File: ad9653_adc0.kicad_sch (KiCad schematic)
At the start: 20 parts, among them J201 142-0701-201, J202 142-0701-201, J203 142-0701-201, J204 142-0701-201, U201 AD9653BCPZ-125

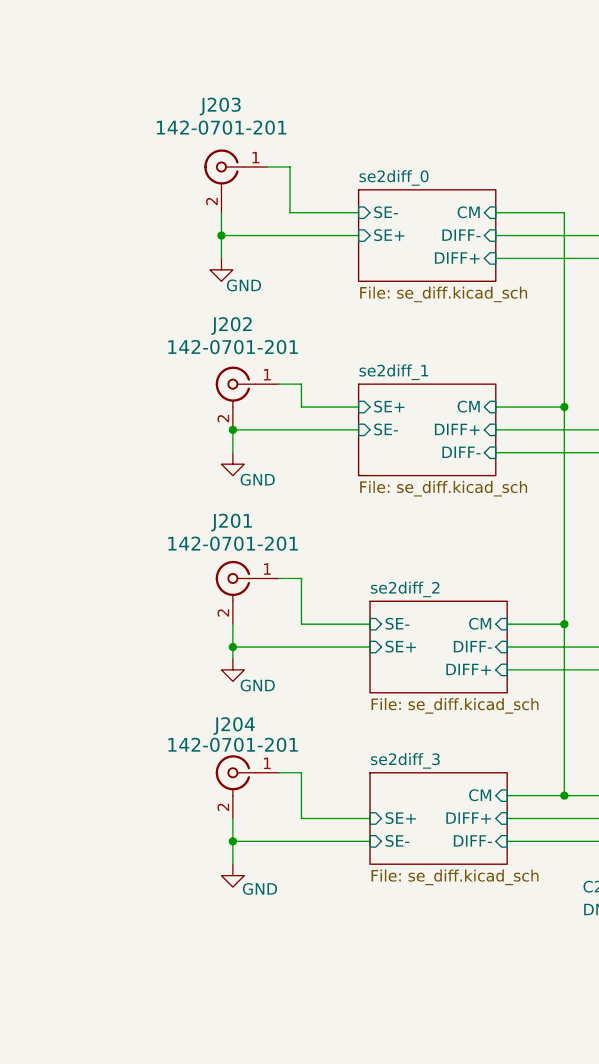
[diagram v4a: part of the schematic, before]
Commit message: Added DC blocking caps and minor layout tweaks
- Adding DC blocking input caps on ADC inputs

-Many minor changes to the layout listed below:
- General silkscreen tweak to avoid text over vias
-Adding pin1 markers on U1002, U2701,U2901,U3101,U3201,U3001,U903
-Adjusted pin1 indicator in footprint on U3002 to be close to part
-Adjusted the size of traces on U2301 to not have trace larger than pin
-Adjusted silkscreen of U1101 to not be underpart and moved pin 1 indicator closer
-Adjusted tracks around c901&R905 to go through center of pads
-Adjusted tracks around r2702&r2701 to go through center of pads
-Fixed some multi-via tracks to connect all vias around PMOD connector on top and in4 layers
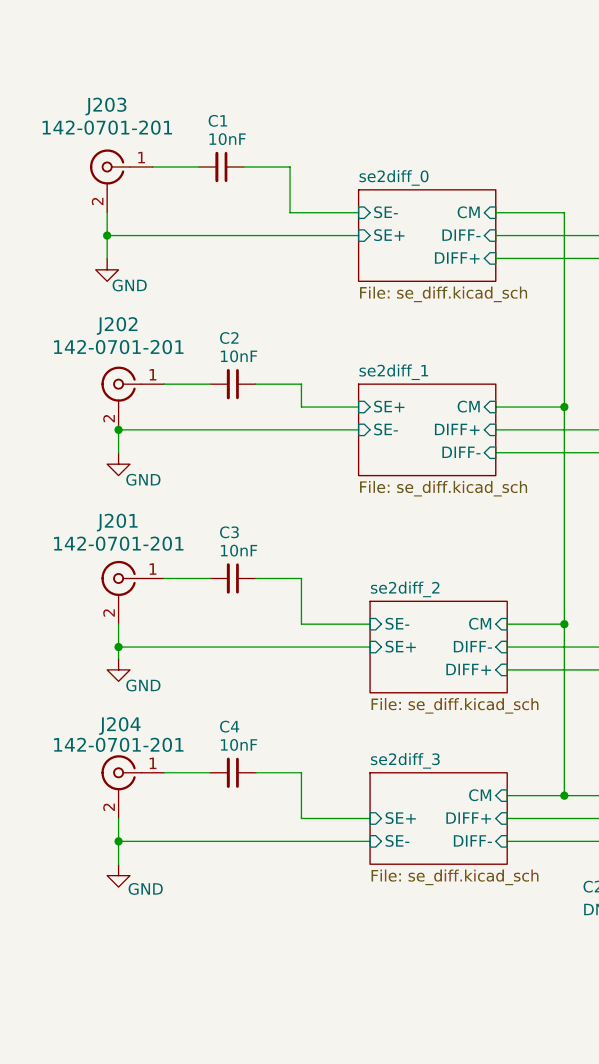
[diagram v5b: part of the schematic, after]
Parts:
- added C1, C2, C3, C4: 10nF, Capacitor_SMD:C_0603_1608Metric, symbol Device:C_Small
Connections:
- net se2diff_0/SE-: now also C1.1; no longer J203.1 (In)
- net se2diff_1/SE+: now also C2.1; no longer J202.1 (In)
- net se2diff_2/SE-: now also C3.1; no longer J201.1 (In)
- net se2diff_3/SE+: now also C4.1; no longer J204.1 (In)
- new net: C1.2, J203.1 (In)
- new net: C2.2, J202.1 (In)
- new net: C4.2, J204.1 (In)
- new net: C3.2, J201.1 (In)
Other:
- moved on the sheet: J201, J202, J203, J204

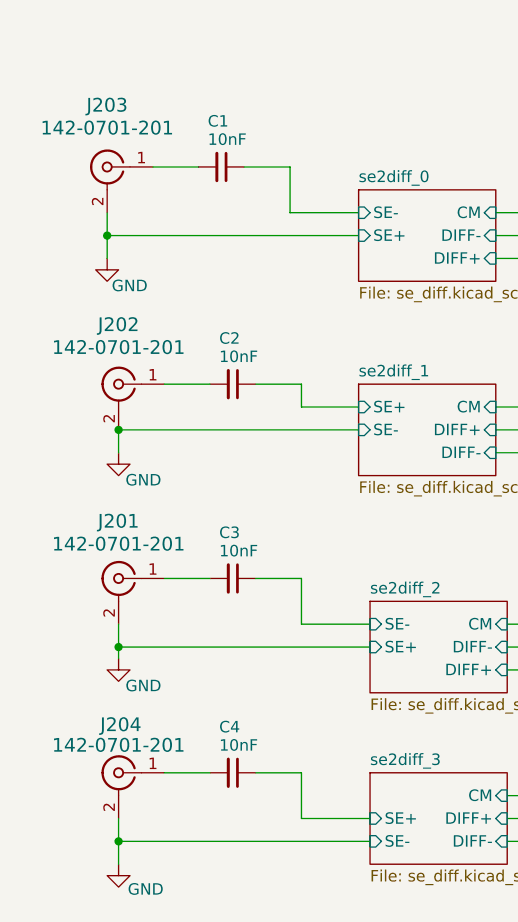
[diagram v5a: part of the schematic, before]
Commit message: Further Project cleanup
-Added BOM and fabrication files
-updated all documentation files
- Added suggested DC blocking cap at DAC outputs

-Set DRC to 5mil trace and space and fixed various violations detailed below
- Removed various small tracks overlapping IC pads on U2701,U2901,U3101,U3201
- Spaced vias 5 mil apart around U701, U201, 1201
- Moved LMK_CLKout3 pair on In4 layer away from PMOD1_1 pin
- adjusted track into pin47 on U701 to clear pin 48
- adjusted trace under U903 to give more room from ground pads/vias
- spaced out vias around pins45/46 of U201

-Many tweak to trace to go through the center of pad throughout the design
-An example is the trace around C3005
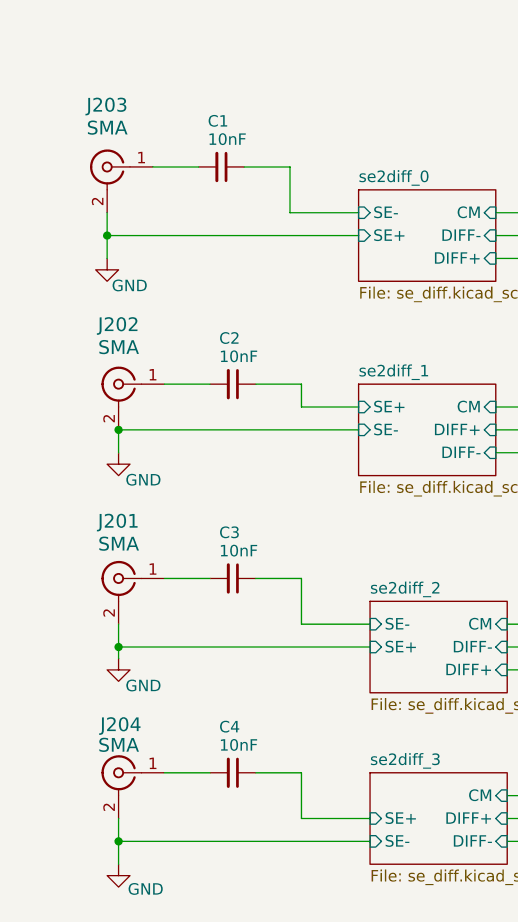
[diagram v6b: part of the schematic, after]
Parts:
- J201, J202, J203, J204: value 142-0701-201 -> SMA
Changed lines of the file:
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@@
 			)
 		)
-		(property "Description" "CAP CER 10nF 25V C0G 0603"
+		(property "Description" "CAP CER 10000PF 25V C0G 0603"
 			(at 118.11 77.47 0)
 			(effects
@@
 			)
 		)
-		(property "Description" "CAP CER 10nF 25V C0G 0603"
+		(property "Description" "CAP CER 10000PF 25V C0G 0603"
 			(at 119.38 101.6 0)
 			(effects
@@
 			)
 		)
-		(property "Description" "CAP CER 10nF 25V C0G 0603"
+		(property "Description" "CAP CER 10000PF 25V C0G 0603"
 			(at 119.38 144.78 0)
 			(effects
@@
 			)
 		)
-		(property "Value" "142-0701-201"
+		(property "Value" "SMA"
 			(at 106.68 141.732 0)
 			(effects
@@
 			)
 		)
-		(property "Description" "CAP CER 10nF 25V C0G 0603"
+		(property "Description" "CAP CER 10000PF 25V C0G 0603"
 			(at 168.91 158.75 0)
 			(effects
@@
 			)
 		)
-		(property "Description" "CAP CER 10nF 25V C0G 0603"
+		(property "Description" "CAP CER 10000PF 25V C0G 0603"
 			(at 119.38 123.19 0)
 			(effects
@@
 			)
 		)
-		(property "Value" "142-0701-201"
+		(property "Value" "SMA"
 			(at 105.41 73.152 0)
 			(effects
@@
 			)
 		)
-		(property "Value" "142-0701-201"
+		(property "Value" "SMA"
 			(at 106.68 97.536 0)
 			(effects
@@
 			)
 		)
-		(property "Value" "142-0701-201"
+		(property "Value" "SMA"
 			(at 106.68 119.38 0)
 			(effects

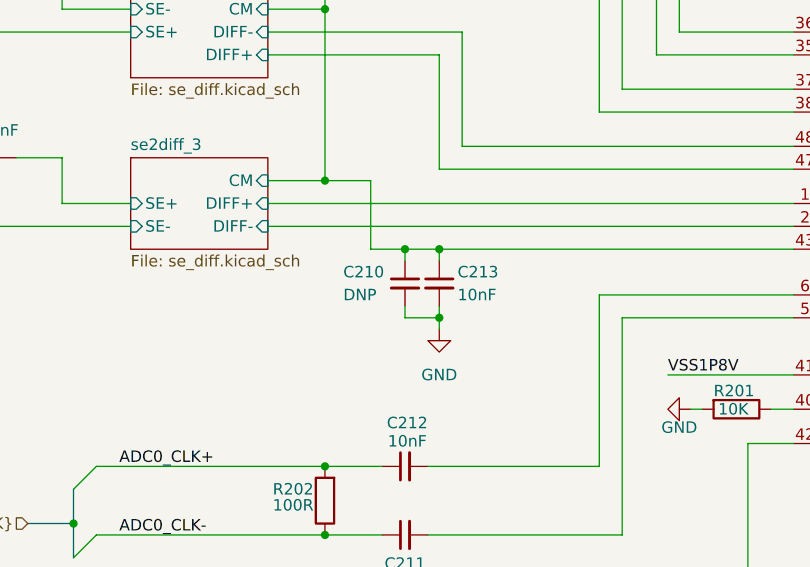
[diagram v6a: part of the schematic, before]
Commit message: Properly attributed DNP parts; Added Fabrication Notes
-Properly attributed various DNP in the project;
This includes: C210.C710,C1601,C2502,C2602,L2501,R1507,L2601,R1601,R805
- I changed the accelerometer and microphone (+it's filter)to DNP parts
  Note: both of these are obsolete parts. As part of this change I Changed R1602 (part of mic buffer) from 220k to 0R. The removal of these parts should in no way negatively effect the rest of the circuit.
-I fixed the 'value' attribute of XMER2501&XMER2601 from 'TC4-6+' -> 'TC4-6T+'
- I added some fabrication notes to the F.Fab Layer
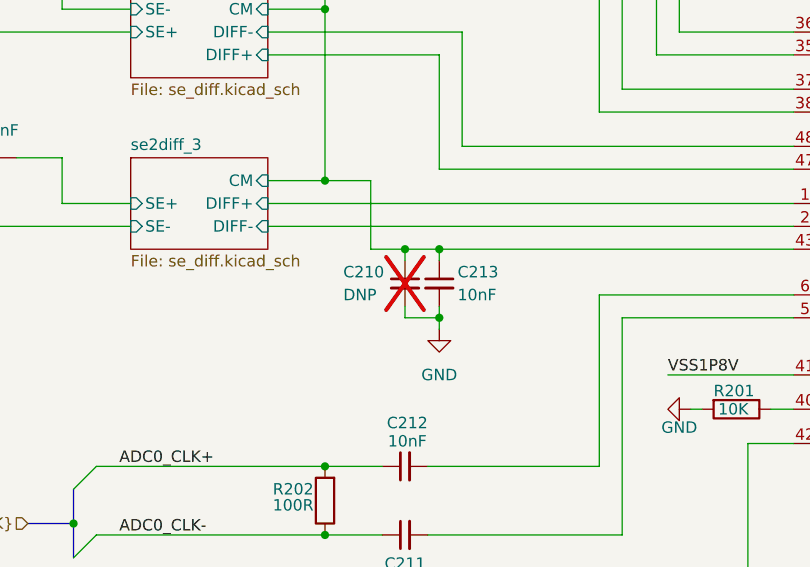
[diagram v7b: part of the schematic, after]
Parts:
- C210: now not fitted
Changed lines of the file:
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@@
 		(in_bom yes)
 		(on_board yes)
-		(dnp no)
+		(dnp yes)
 		(property "Reference" "C210"
 			(at 158.242 157.48 0)

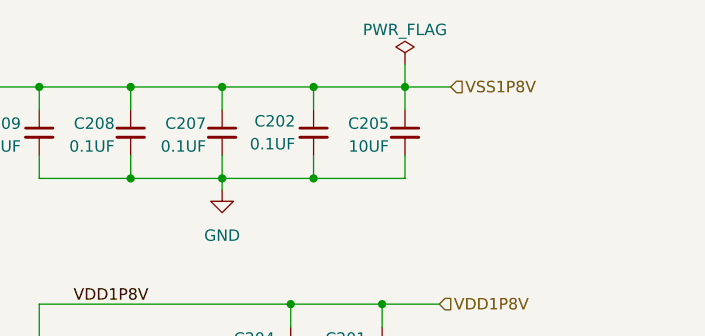
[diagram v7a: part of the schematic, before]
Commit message: resolve duplicate power flag
kicad 8 complains about two power flags on VSS1P8V net,
one each on ADC0 and ADC1 pages.  Consolidate to one
flag on the U35_LT6233 page.
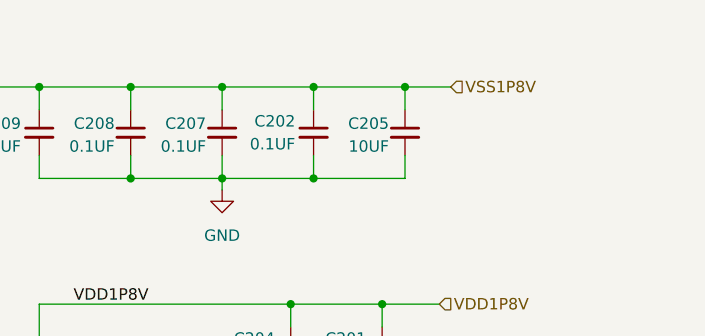
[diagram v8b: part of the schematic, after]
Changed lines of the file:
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@@
 	(wire
 		(pts
-			(xy 276.86 66.04) (xy 276.86 68.58)
-		)
-		(stroke
-			(width 0)
-			(type default)
-		)
-	)
-	(wire
-		(pts
 			(xy 256.54 156.21) (xy 288.29 156.21)
 		)
@@
 					(unit 1)
 				)
-			)
-		)
-	)
-	(symbol
-		(lib_id "power:PWR_FLAG")
-		(at 276.86 66.04 0)
-		(mirror y)
-		(unit 1)
-		(exclude_from_sim no)
-		(in_bom yes)
-		(on_board yes)
-		(dnp no)
-		(property "Reference" "#FLG04"
-			(at 276.86 64.135 0)
-			(effects
-				(font
-					(size 1.27 1.27)
-				)
-				(hide yes)
-			)
-		)
-		(property "Value" "PWR_FLAG"
-			(at 276.86 62.23 0)
-			(effects
-				(font
-					(size 1.27 1.27)
-				)
-			)
-		)
-		(property "Footprint" ""
-			(at 276.86 66.04 0)
-			(effects
-				(font
-					(size 1.27 1.27)
-				)
-				(hide yes)
-			)
-		)
-		(property "Datasheet" "~"
-			(at 276.86 66.04 0)
-			(effects
-				(font
-					(size 1.27 1.27)
-				)
-				(hide yes)
-			)
-		)
-		(property "Description" "Special symbol for telling ERC where power comes from"
-			(at 276.86 66.04 0)
-			(effects
-				(font
-					(size 1.27 1.27)
-				)
-				(hide yes)
-			)
-		)
-		(pin "1"
-		)
-		(instances
-			(project "zest"
-				(path "/00000000-0000-0000-0000-000000000003/00000000-0000-0000-0000-000000000000"
-					(reference "#FLG04")
-					(unit 1)
-				)
